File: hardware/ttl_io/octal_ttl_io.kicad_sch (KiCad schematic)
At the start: 64 parts, among them J10 Conn_Coaxial, J11 Conn_Coaxial, J12 Conn_Coaxial, J4 Conn_Coaxial, J6 Conn_Coaxial, J7 Conn_Coaxial, J8 Conn_Coaxial, J9 Conn_Coaxial, U10 74LVCH2T45DC, U11 74LVCH2T45DC, U12 74LVCH2T45DC, U13 74LVCH2T45DC, U5 74LVCH2T45DC, U6 74LVCH2T45DC, U7 74LVCH2T45DC, U9 74LVCH2T45DC

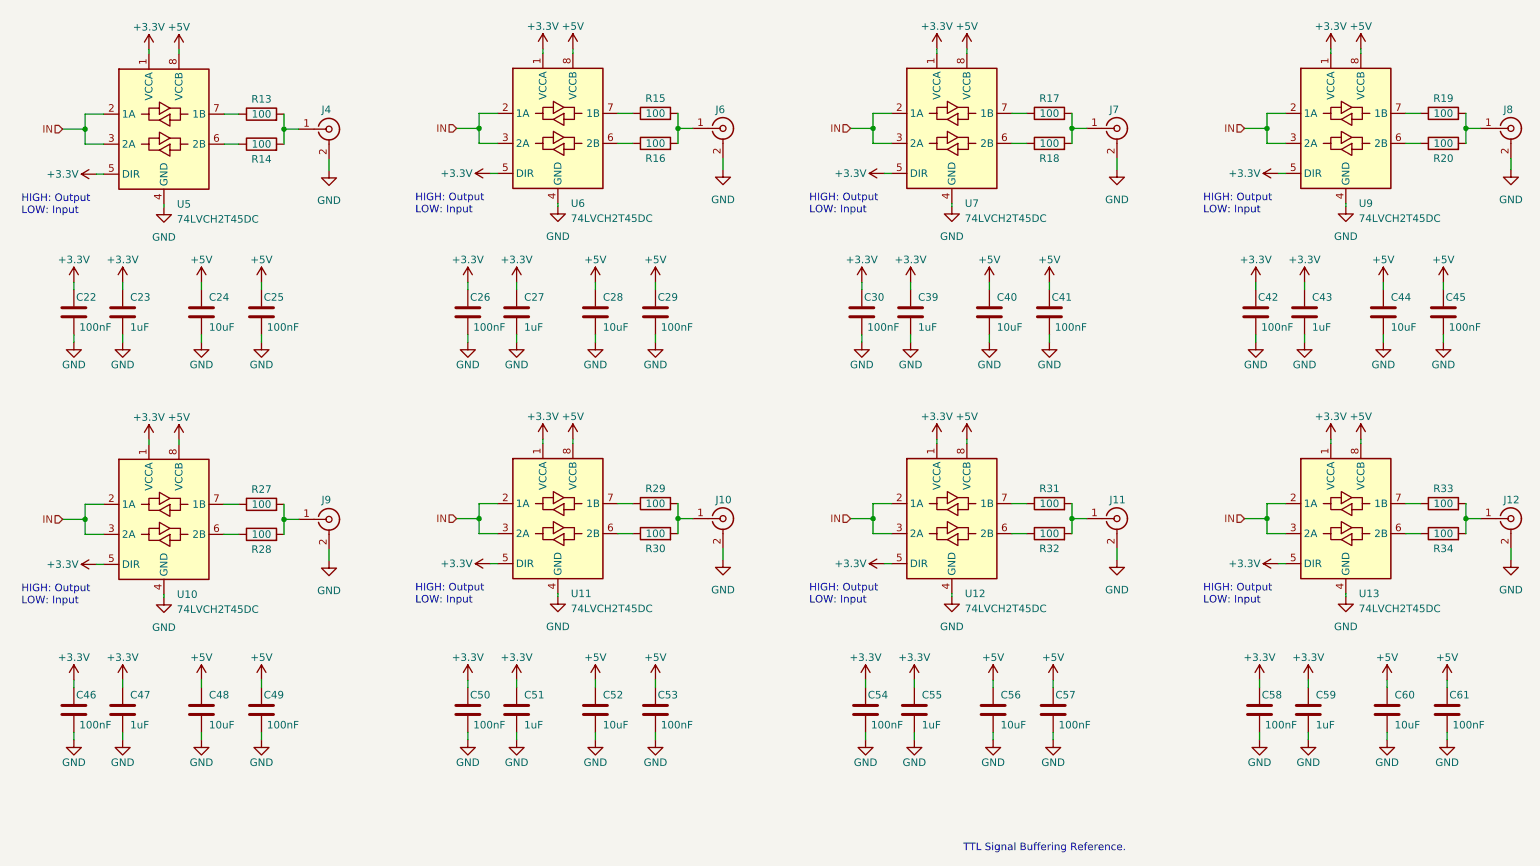
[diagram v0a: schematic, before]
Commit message: draft mcu bypass with bus switches
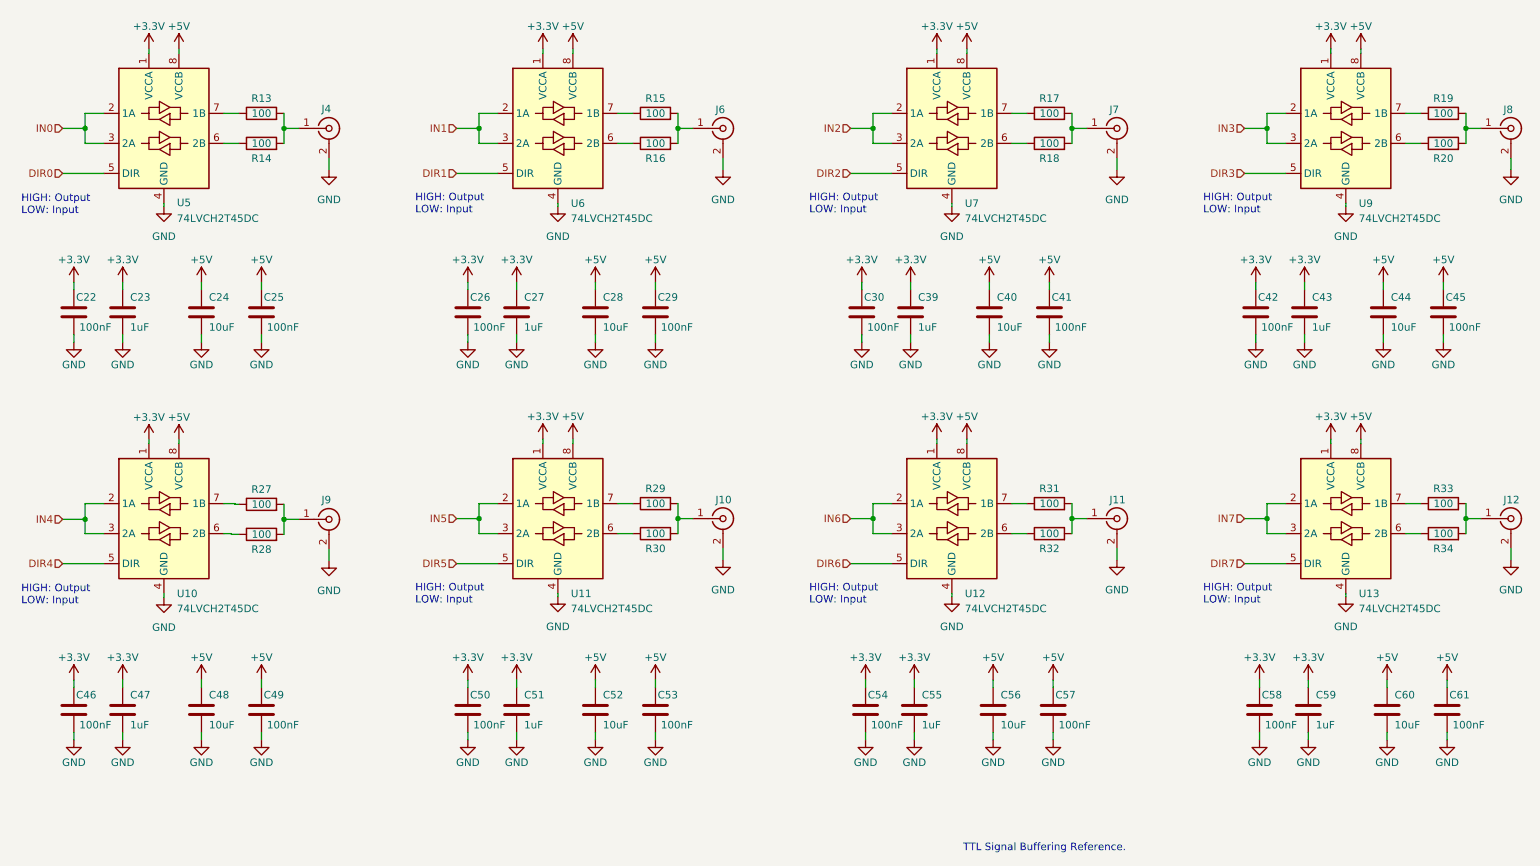
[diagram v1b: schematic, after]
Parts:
- J10, J11, J12, J4, J6, J7, J8, J9: footprint kicad_component_library:SMA_TE_Connectivity_CONSMA002-SMD-G-T_Horizontal -> (none)
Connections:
- net +3V3: no longer U10.5 (DIR), U11.5 (DIR), U12.5 (DIR), U13.5 (DIR), U5.5 (DIR), U6.5 (DIR), U7.5 (DIR), U9.5 (DIR)
- removed net IN: U10.2 (1A), U10.3 (2A), U11.2 (1A), U11.3 (2A), U12.2 (1A), U12.3 (2A), U13.2 (1A), U13.3 (2A), U5.2 (1A), U5.3 (2A), U6.2 (1A), U6.3 (2A), U7.2 (1A), U7.3 (2A), U9.2 (1A), U9.3 (2A)
- new net DIR0: U5.5 (DIR)
- new net DIR1: U6.5 (DIR)
- new net DIR2: U7.5 (DIR)
- new net DIR3: U9.5 (DIR)
- new net DIR4: U10.5 (DIR)
- new net DIR5: U11.5 (DIR)
- new net DIR6: U12.5 (DIR)
- new net DIR7: U13.5 (DIR)
- new net IN0: U5.2 (1A), U5.3 (2A)
- new net IN1: U6.2 (1A), U6.3 (2A)
- new net IN2: U7.2 (1A), U7.3 (2A)
- new net IN3: U9.2 (1A), U9.3 (2A)
- new net IN4: U10.2 (1A), U10.3 (2A)
- new net IN5: U11.2 (1A), U11.3 (2A)
- new net IN6: U12.2 (1A), U12.3 (2A)
- new net IN7: U13.2 (1A), U13.3 (2A)

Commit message: update passthrough level translator
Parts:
- J10, J11, J12, J6, J7, J8, J9: footprint (none) -> kicad_component_library:BNC_TEConnectivity_CONBNC001_Vertical; Link https://www.digikey.com/en/products/detail/te-connectivity-linx/CONSMA002-SMD-G-T/10524518 -> https://www.digikey.com/en/products/detail/te-connectivity-linx/CONBNC001/16013844?; Manufacturer Number CONSMA002-SMD-G-T -> CONBNC001
- J5: renamed from J4; footprint (none) -> kicad_component_library:BNC_TEConnectivity_CONBNC001_Vertical; Link https://www.digikey.com/en/products/detail/te-connectivity-linx/CONSMA002-SMD-G-T/10524518 -> https://www.digikey.com/en/products/detail/te-connectivity-linx/CONBNC001/16013844?; Manufacturer Number CONSMA002-SMD-G-T -> CONBNC001

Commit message: update layout
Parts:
- R13, R14, R15, R16, R17, R18, R19, R20, R27, R28, R29, R30, R31, R32, R33, R34: footprint Resistor_SMD:R_0603_1608Metric_Pad0.98x0.95mm_HandSolder -> Resistor_SMD:R_0402_1005Metric; Link https://www.digikey.com/en/products/detail/yageo/SR0603FR-7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 -> https://www.digikey.com/en/products/detail/koa-speer-electr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; Manufacturer Yageo -> KOA Speer Electronics, Inc.; Manufacturer Number SR0603FR-7T100RL -> SG73P1EWTTP1000F

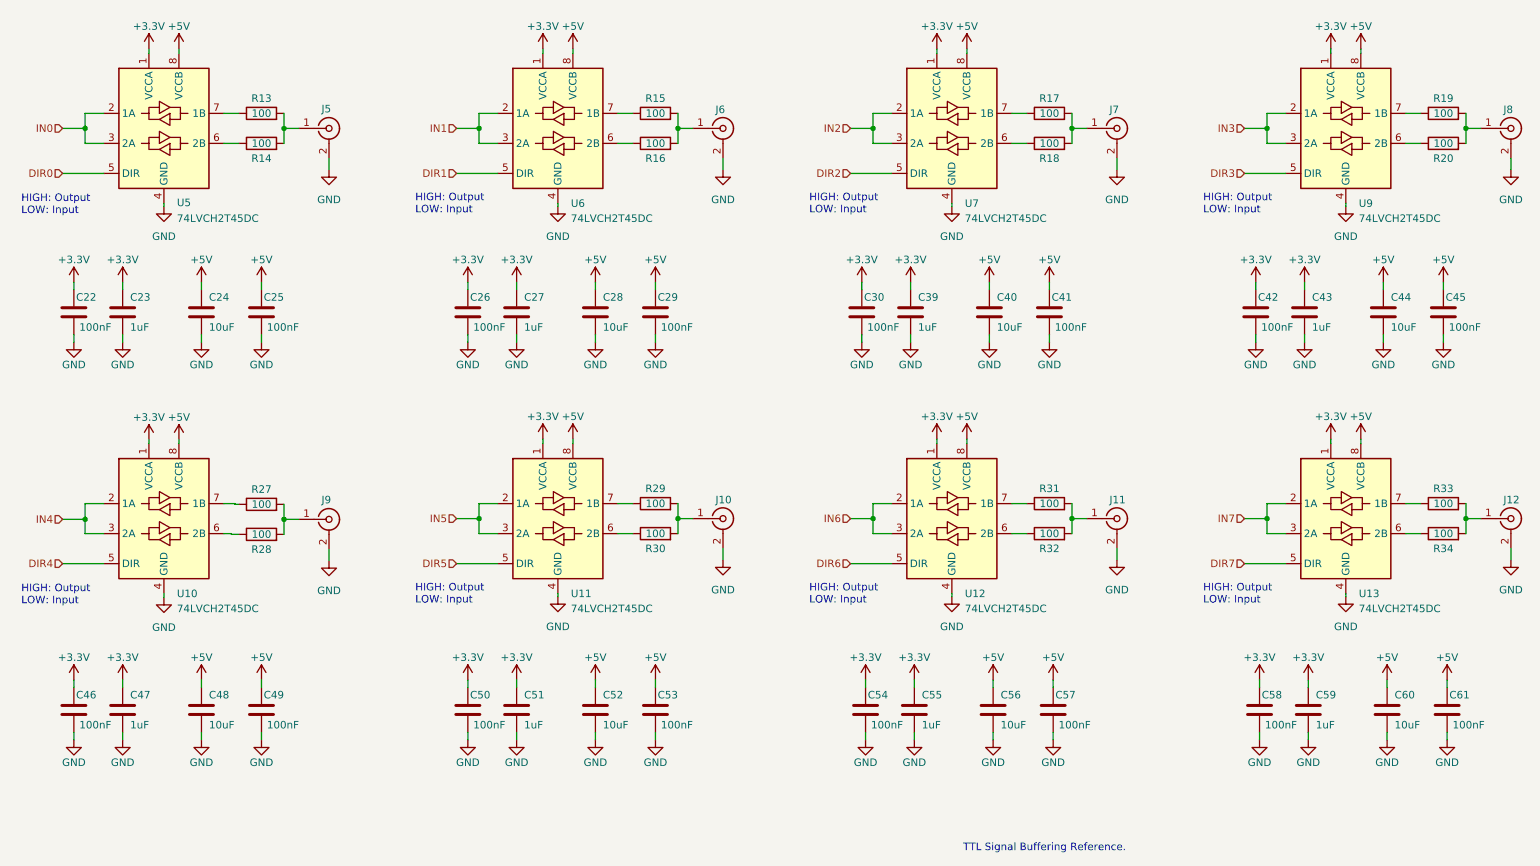
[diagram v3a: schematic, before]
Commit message: update power supply schematic/board
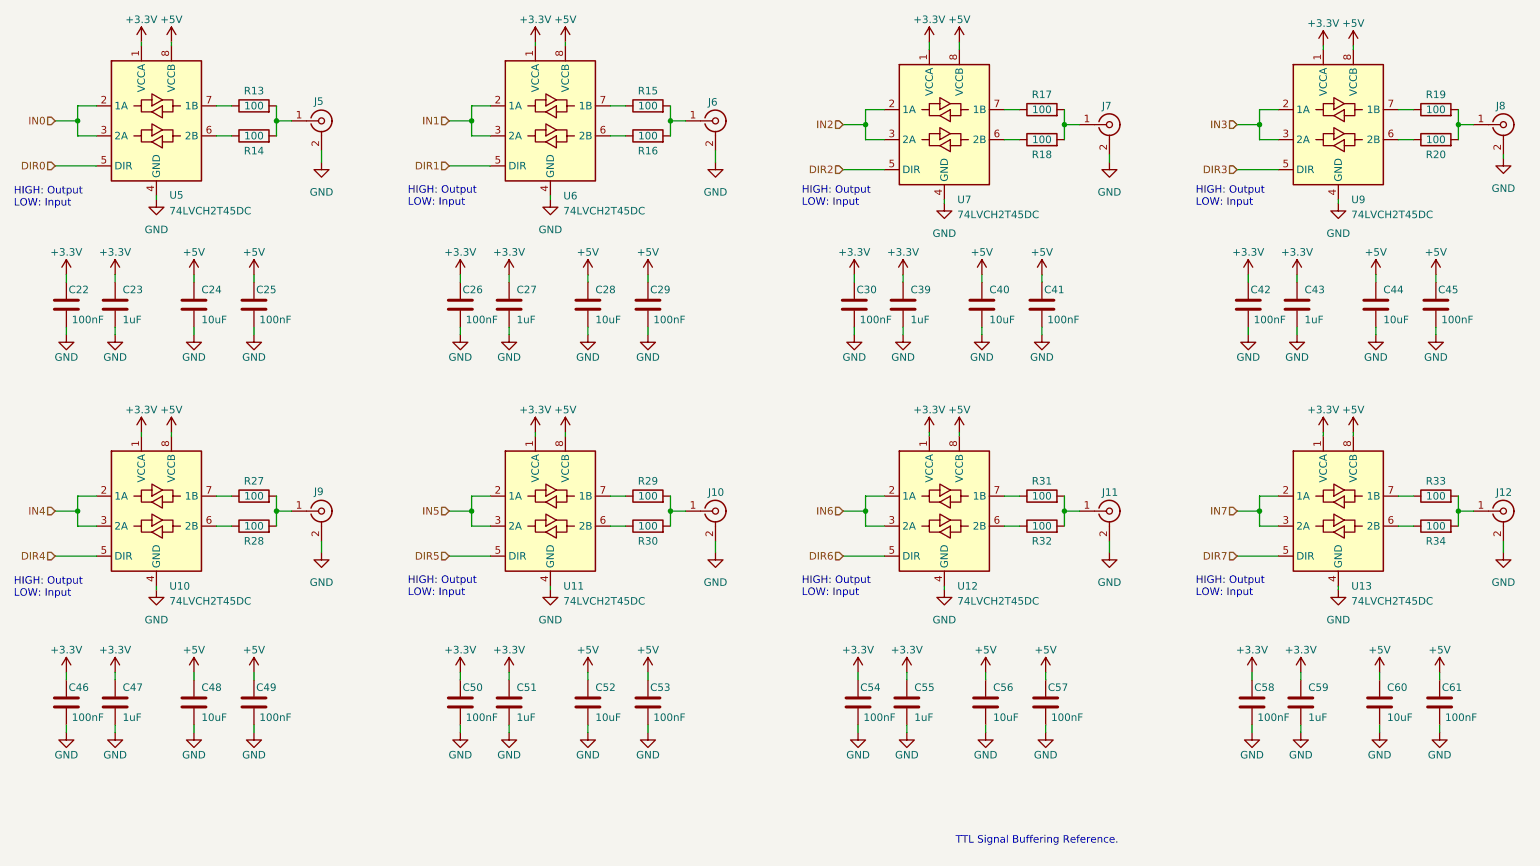
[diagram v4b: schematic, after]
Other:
- moved on the sheet: C22, C23, C24, C25, C26, C27, C28, C29, C30, C39, C40, C41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

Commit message: update pcb and bom
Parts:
- J10, J11, J12, J5, J6, J7, J8, J9: footprint kicad_component_library:BNC_TEConnectivity_CONBNC001_Vertical -> kicad_component_library:BNC_AmphenolRF_031-5329-52RFX_Vertical; Link https://www.digikey.com/en/products/detail/te-connectivity-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 -> https://www.digikey.com/en/products/detail/amphenol-rf/031-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; Manufacturer TE Connectivity Linx -> Amphenol RF; Manufacturer Number CONBNC001 -> 031-5329-52RFX
